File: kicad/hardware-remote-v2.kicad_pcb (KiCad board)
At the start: 2 copper layers, 130 x 70 mm, 25 parts, among them J1 Flash, J2 TFT, J3 5VIN, J4 3.3VIN, J5 Conn_02x08_Odd_Even, Q1 SI2301CDS-T1-GE3, SW1 ANALOG_LEFT, SW2 ANALOG_RIGHT, U1 ESP32-WROOM-32, U2 AMS1117-3.3

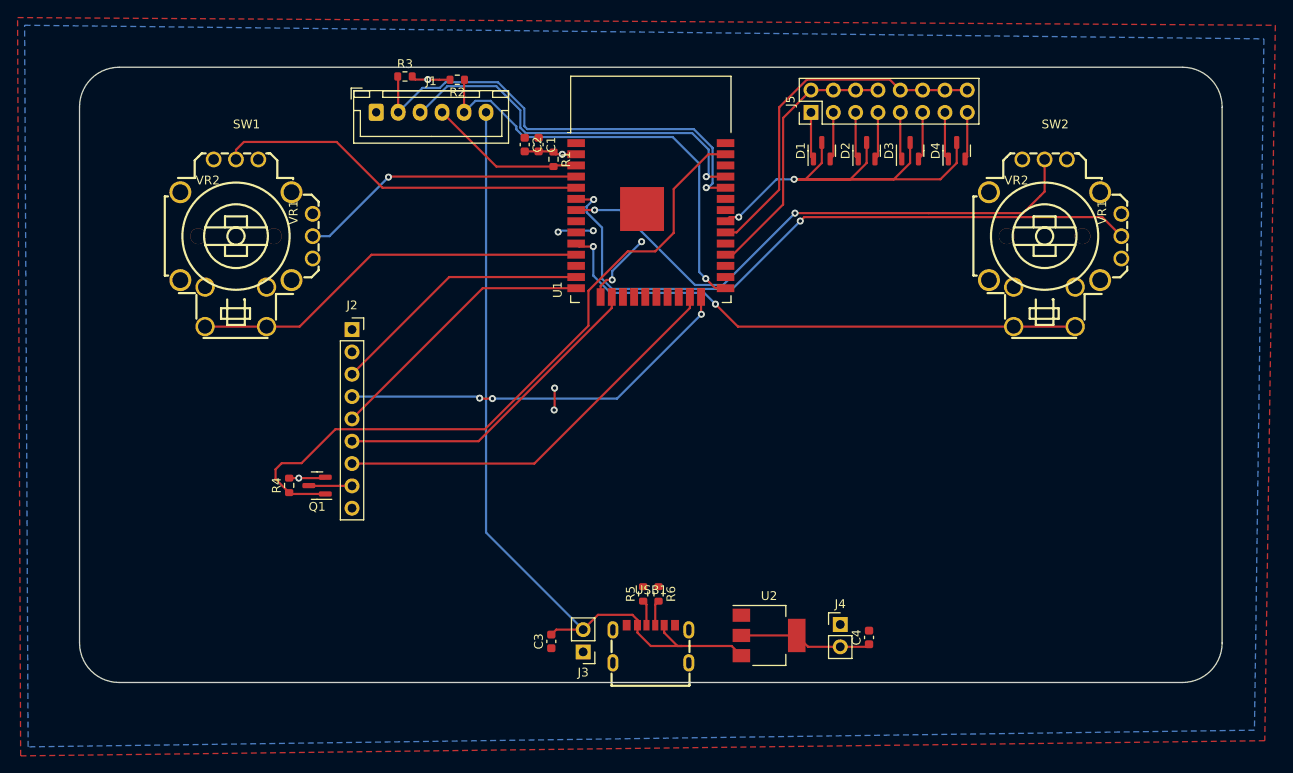
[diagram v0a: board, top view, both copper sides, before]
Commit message: Updated usb, still needs someone to put flasher on there
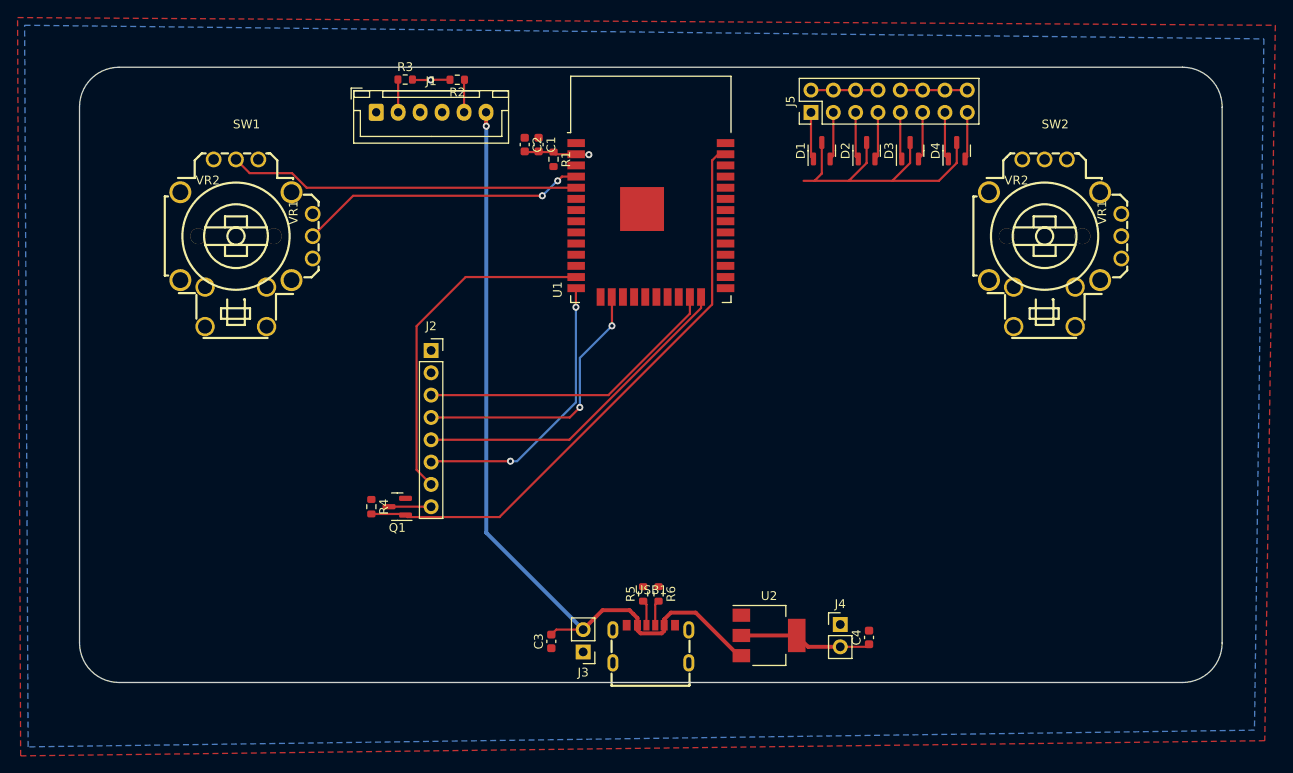
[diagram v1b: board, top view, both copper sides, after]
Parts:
- J2: footprint Connector_PinSocket_2.54mm:PinSocket_1x09_P2.54mm_Vertical -> Connector_PinSocket_2.54mm:PinSocket_1x08_P2.54mm_Vertical
- Q1: value SI2301CDS-T1-GE3 -> 2N7002
- R4: value 2k2 -> 10k
- moved R4 9.66 mm to (-31.8, 10.0), turned to -90 degrees
- moved Q1 9.44 mm to (-28.9, 10.0)
- moved J2 9.31 mm to (-25.0, -7.78)
- moved R3 0.35 mm to (-27.9, -38.6)
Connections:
- J2 pad 1: +3V3 -> GND
- J2 pad 2: GND -> +3V3
- J2 pad 3: CS -> TFT_SCLK
- J2 pad 4: TFT_RESET -> TFT_MOSI
- J2 pad 5: TFT_DC -> TFT_RESET
- J2 pad 6: TFT_MOSI -> TFT_DC
- J2 pad 7: TFT_SCLK -> CS
- Q1 pad 2: +3V3 -> GND
- R4 pad 1: TFT_LED -> GND
- R4 pad 2: +3V3 -> TFT_LED
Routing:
- net ANALOG_RIGHT_X: track 76.0 -> 0.00 mm, vias 2 -> 0
- net ANALOG_RIGHT_Y: track 64.9 -> 0.00 mm, vias 2 -> 0
- net ANALOG_RIGHT_BUTTON: track 62.6 -> 0.00 mm, vias 2 -> 0
- net ESP_RX: track 52.7 -> 3.74 mm, vias 1 -> 0
- net IO0: track 50.3 -> 3.72 mm, vias 1 -> 0
- net ANALOG_LEFT_BUTTON: track 45.6 -> 0.00 mm
- net ESP_TX: track 43.6 -> 0.00 mm, vias 1 -> 0
- net BUTTON_IN_2: track 40.7 -> 7.62 mm
- net BUTTON_OUT: track 65.3 -> 35.7 mm, vias 2 -> 0
- net BUTTON_IN_1: track 30.9 -> 7.62 mm
- net EN: track 17.9 -> 0.00 mm
- net GND: track 12.7 -> 0.00 mm, vias 4 -> 0
- net TFT_SCLK: track 47.0 -> 35.2 mm
- net TFT_LED: track 78.8 -> 67.1 mm
- net CS: track 30.1 -> 39.2 mm
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
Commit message: PCB Version Beta 0.1
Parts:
- added C5: 100n, Capacitor_SMD:C_0603_1608Metric, F.Cu at (20.3, -13.7)
- added C6: 100n, Capacitor_SMD:C_0603_1608Metric, F.Cu at (18.2, -23.6)
- added C7: 1u, Capacitor_SMD:C_0603_1608Metric, F.Cu at (20.4, -23.1)
- added U3: CH343G, Package_SO:SOIC-16_3.9x9.9mm_P1.27mm, F.Cu at (22.9, -18.3)
- R3: value 1k -> 10k
- U1: value ESP32-WROOM-32 -> ESP32-WROOM-32E-8MB
- USB1: value U262-061N-4BVC11 -> KH-TYPE-C-16P; footprint usb_c_bobby:USB-SMD_U262-061N-4BVC11 -> usb_c_bobby:USB-C-SMD_KH-TYPE-C-16P
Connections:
- USB1 pad A5: Net-(R6-Pad2) -> Net-(R5-Pad1)
- USB1 pad B5: Net-(R5-Pad1) -> Net-(R6-Pad2)
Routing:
- net ANALOG_RIGHT_Y: track 0.00 -> 116.2 mm, vias 0 -> 6
- net ANALOG_RIGHT_X: track 0.00 -> 97.8 mm, vias 0 -> 6
- net +5V: track 91.9 -> 174.0 mm, vias 1 -> 2
- net IO0: track 3.72 -> 72.4 mm, vias 0 -> 4
- net ESP_RX: track 3.74 -> 67.3 mm, vias 0 -> 3
- net ESP_TX: track 0.00 -> 62.7 mm, vias 0 -> 1
- net USB_DN: track 0.00 -> 61.4 mm, vias 0 -> 2
- net ANALOG_RIGHT_BUTTON: track 0.00 -> 60.7 mm, vias 0 -> 4
- net EN: track 0.00 -> 60.1 mm, vias 0 -> 2
- net USB_DP: track 0.00 -> 59.5 mm, vias 0 -> 2
- net ANALOG_LEFT_BUTTON: track 0.00 -> 45.6 mm
- net BUTTON_IN_2: track 7.62 -> 47.4 mm, vias 0 -> 1
- net GND: track 0.00 -> 32.9 mm, vias 0 -> 13
- net BUTTON_IN_1: track 7.62 -> 31.4 mm, vias 0 -> 1
- net BUTTON_OUT: track 35.7 -> 47.0 mm, vias 0 -> 2
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
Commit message: Fixed DRC
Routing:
- net GND: track 32.9 -> 80.8 mm, vias 13 -> 31
- net +3V3: track 33.8 -> 57.0 mm, vias 5 -> 18
- net USB_DN: track 61.4 -> 63.9 mm
- net EN: track 60.1 -> 59.3 mm

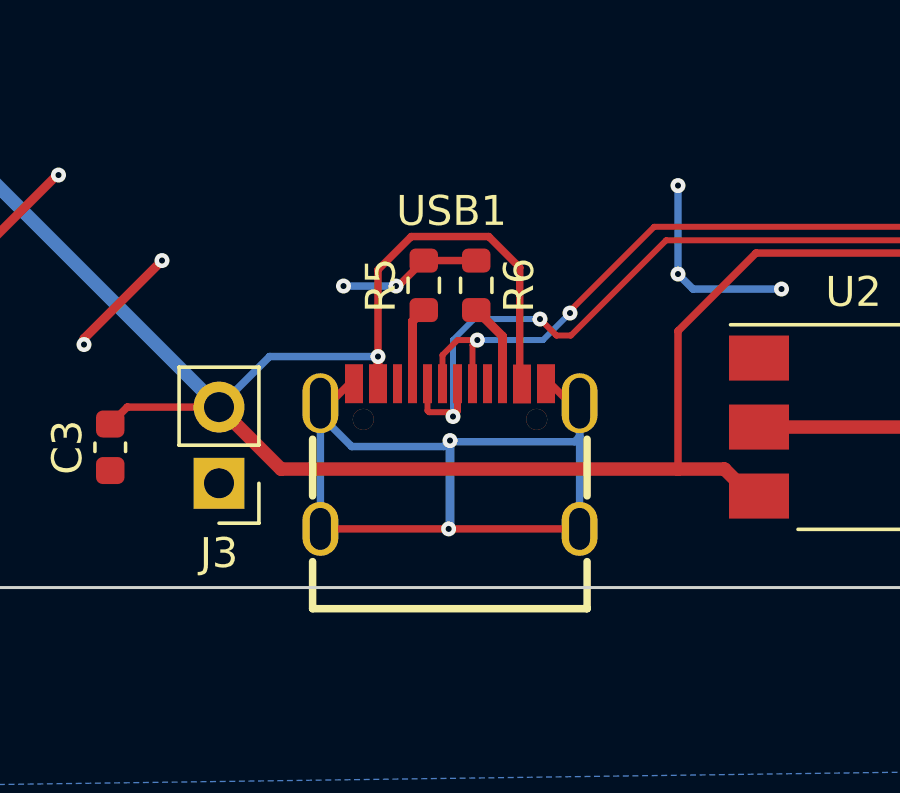
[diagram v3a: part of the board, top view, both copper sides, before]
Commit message: Actually use usb c that they can solder
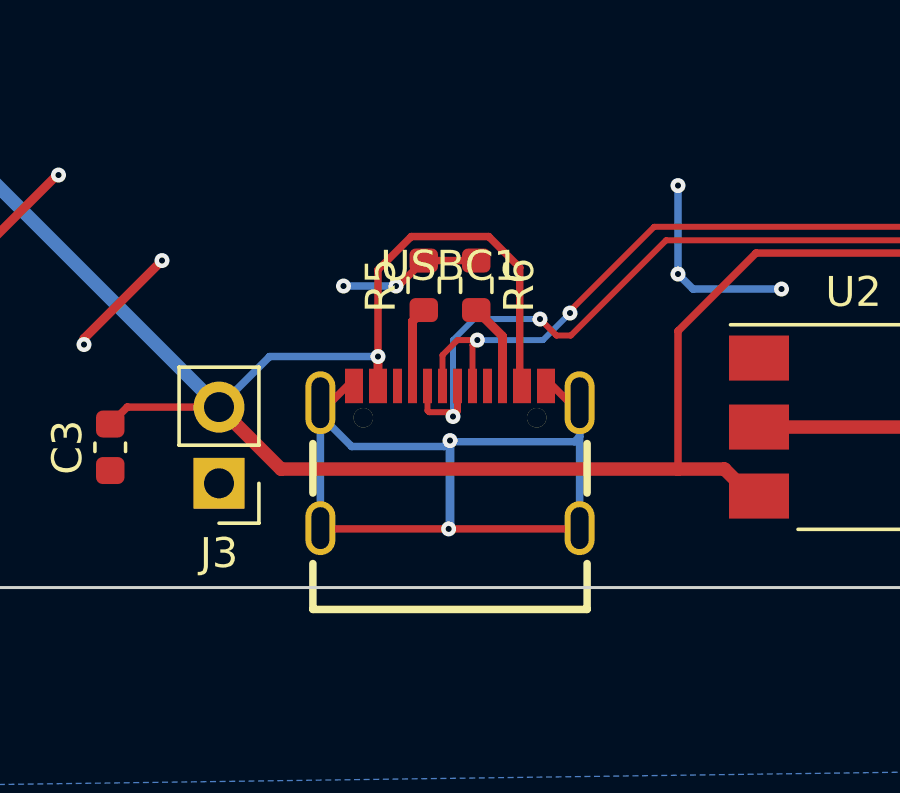
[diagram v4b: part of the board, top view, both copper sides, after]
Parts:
- removed USB1: KH-TYPE-C-16P, usb_c_bobby:USB-C-SMD_KH-TYPE-C-16P
- added USBC1: MC-311D, usb_c_bobby:USB-C-SMD_MC-311D, F.Cu at (0.00, 25.6)
